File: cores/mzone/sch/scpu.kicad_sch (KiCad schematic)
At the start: 33 parts, among them X1 14.318MHZ

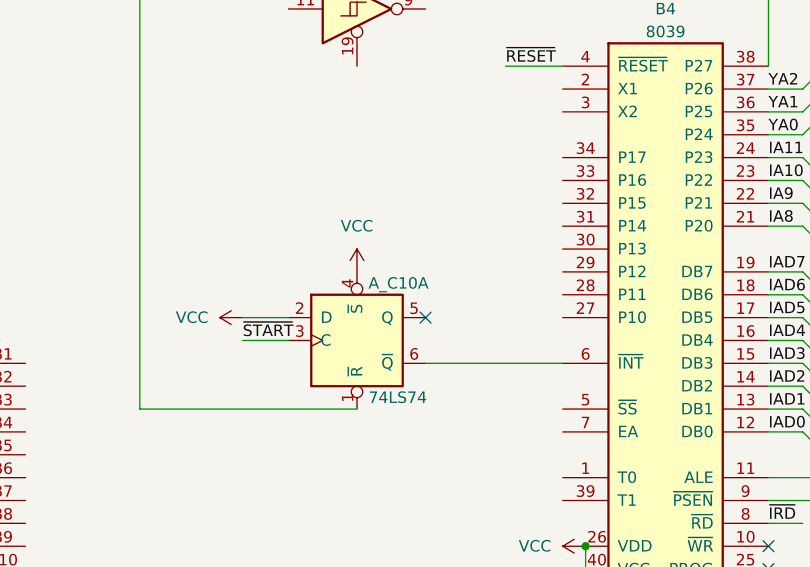
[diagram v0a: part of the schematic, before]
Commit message: mzone core
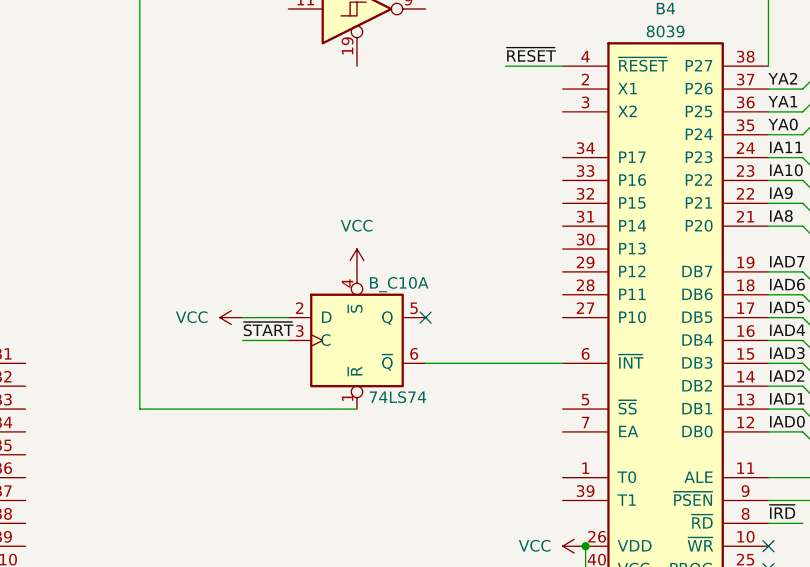
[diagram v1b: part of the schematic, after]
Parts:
- renumbered A_C10 to B_C10
